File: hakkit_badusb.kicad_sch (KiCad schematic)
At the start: 22 parts, among them J1 USB3_A, J2 Micro_SD_Card, SW1 SW_Push, U1 RP2040, U2 W25Q128JVP, U3 LT1962-3.3, Y1 12MHz Cryst

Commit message: remade pcb
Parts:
- J2: footprint (none) -> Connector_Card:microSD_HC_Molex_47219-2001
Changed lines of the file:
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@@
 			)
 		)
-		(property "Footprint" ""
+		(property "Footprint" "Connector_Card:microSD_HC_Molex_47219-2001"
 			(at 289.56 107.95 0)
 			(hide yes)

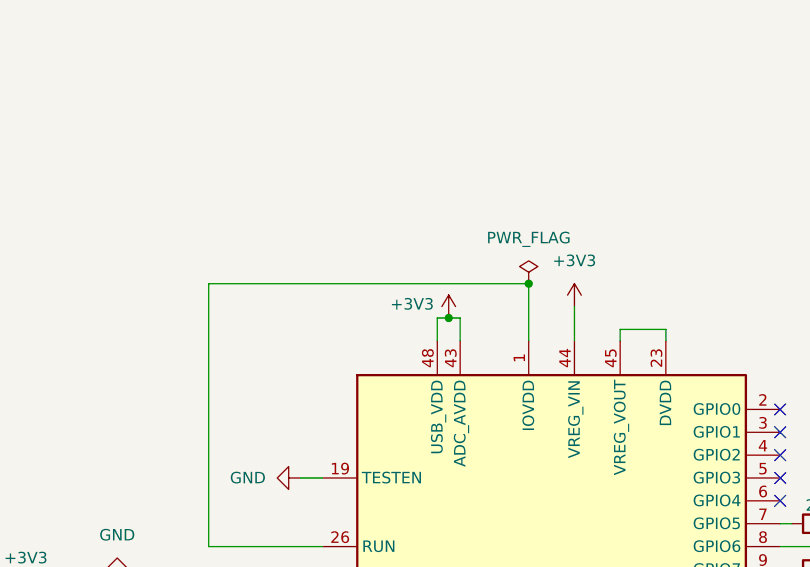
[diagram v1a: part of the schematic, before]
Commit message: finished board | must redo cause of components unaiavalbility
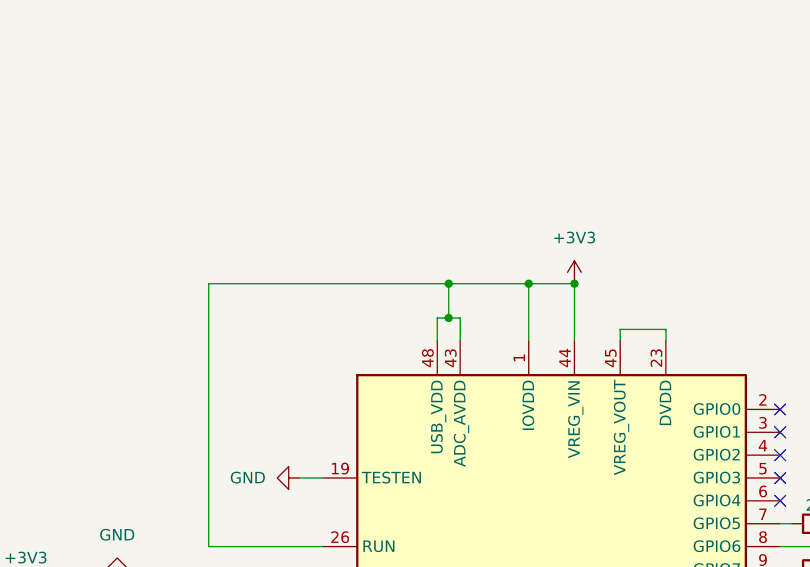
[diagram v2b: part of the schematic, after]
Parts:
- C1, C2, C4, C5, C6: footprint C_0603_1608Metric -> Capacitor_SMD:C_0603_1608Metric
- SW1: footprint (none) -> Button_Switch_SMD:SW_Push_1P1T_NO_CK_KMR2
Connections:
- net +3V3: now also U1.1 (IOVDD), U1.10 (IOVDD), U1.22 (IOVDD), U1.26 (RUN), U1.33 (IOVDD), U1.42 (IOVDD), U1.49 (IOVDD)
